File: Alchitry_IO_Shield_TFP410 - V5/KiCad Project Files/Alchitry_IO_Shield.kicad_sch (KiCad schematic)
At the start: 1 part, among them U1 boardmezzanine_new

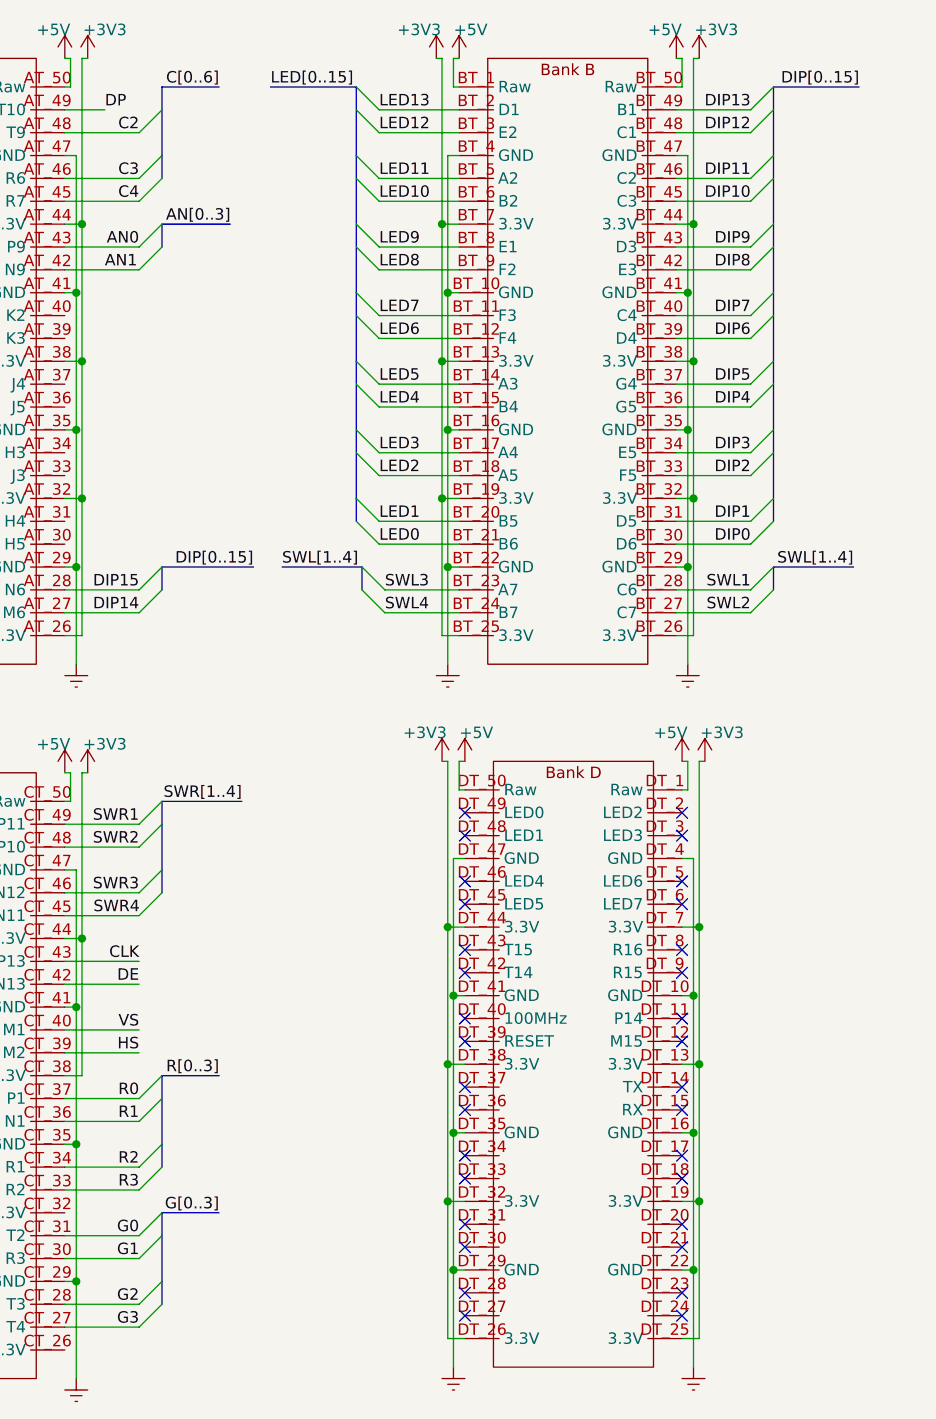
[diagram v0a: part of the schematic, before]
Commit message: grouped footprints by function
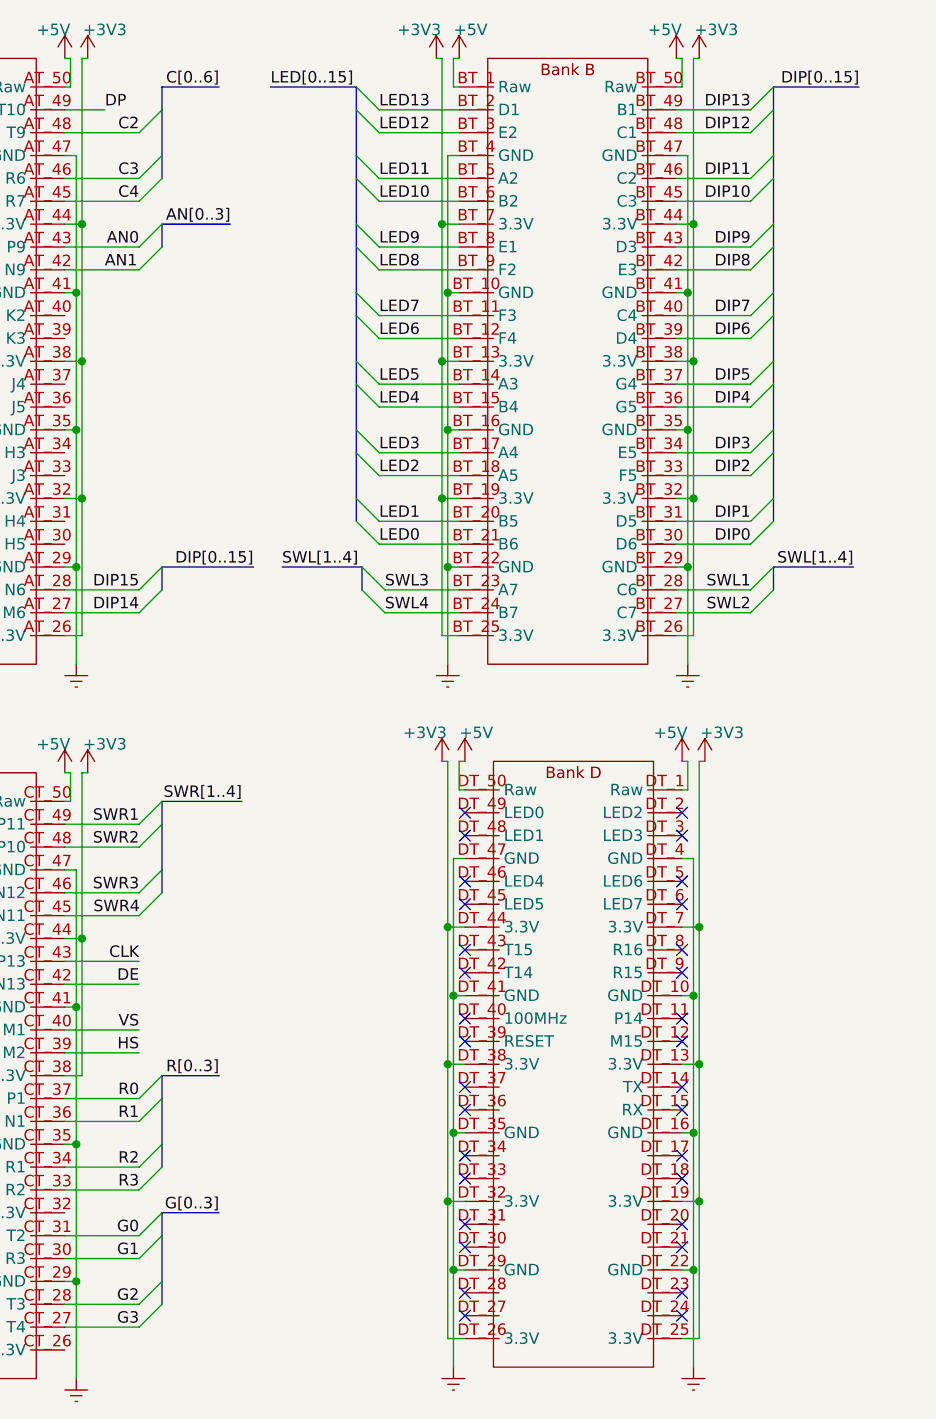
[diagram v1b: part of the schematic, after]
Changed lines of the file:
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@@
-(kicad_sch (version 20200714) (host eeschema "(5.99.0-2326-ge7e1d5140)")
+(kicad_sch (version 20200714) (host eeschema "(5.99.0-2416-g010316457)")
   (page 1 3)
   (paper "A4")
@@
   (junction (at 135.255 129.54) (diameter 0) (color 0 0 0 0))
   (junction (at 135.255 144.78) (diameter 0) (color 0 0 0 0))
+  (no_connect (at 133.35 111.76))
+  (no_connect (at 133.35 104.14))
+  (no_connect (at 109.22 119.38))
+  (no_connect (at 40.64 143.51))
+  (no_connect (at 133.35 116.84))
+  (no_connect (at 109.22 104.14))
+  (no_connect (at 133.35 157.48))
+  (no_connect (at 40.64 133.35))
+  (no_connect (at 109.22 124.46))
+  (no_connect (at 109.22 132.08))
+  (no_connect (at 109.22 134.62))
+  (no_connect (at 109.22 109.22))
+  (no_connect (at 40.64 140.97))
+  (no_connect (at 109.22 101.6))
+  (no_connect (at 133.35 147.32))
+  (no_connect (at 40.64 102.87))
+  (no_connect (at 109.22 157.48))
+  (no_connect (at 109.22 154.94))
   (no_connect (at 133.35 134.62))
+  (no_connect (at 133.35 132.08))
+  (no_connect (at 133.35 101.6))
+  (no_connect (at 109.22 149.86))
+  (no_connect (at 109.22 127))
+  (no_connect (at 133.35 127))
   (no_connect (at 40.64 120.65))
-  (no_connect (at 109.22 127))
-  (no_connect (at 133.35 111.76))
-  (no_connect (at 133.35 132.08))
+  (no_connect (at 109.22 116.84))
+  (no_connect (at 133.35 124.46))
+  (no_connect (at 40.64 125.73))
+  (no_connect (at 40.64 113.03))
   (no_connect (at 40.64 128.27))
+  (no_connect (at 133.35 119.38))
+  (no_connect (at 40.64 135.89))
+  (no_connect (at 133.35 149.86))
+  (no_connect (at 40.64 118.11))
+  (no_connect (at 133.35 154.94))
+  (no_connect (at 40.64 110.49))
+  (no_connect (at 133.35 139.7))
+  (no_connect (at 40.64 105.41))
+  (no_connect (at 133.35 142.24))
+  (no_connect (at 109.22 139.7))
   (no_connect (at 109.22 147.32))
+  (no_connect (at 109.22 142.24))
   (no_connect (at 109.22 111.76))
-  (no_connect (at 133.35 157.48))
-  (no_connect (at 109.22 116.84))
-  (no_connect (at 133.35 142.24))
   (no_connect (at 133.35 109.22))
-  (no_connect (at 109.22 139.7))
-  (no_connect (at 40.64 110.49))
-  (no_connect (at 133.35 101.6))
-  (no_connect (at 109.22 142.24))
-  (no_connect (at 133.35 119.38))
-  (no_connect (at 109.22 104.14))
-  (no_connect (at 109.22 154.94))
-  (no_connect (at 40.64 118.11))
-  (no_connect (at 109.22 119.38))
-  (no_connect (at 109.22 134.62))
-  (no_connect (at 133.35 116.84))
-  (no_connect (at 40.64 102.87))
-  (no_connect (at 40.64 133.35))
-  (no_connect (at 40.64 125.73))
-  (no_connect (at 133.35 124.46))
-  (no_connect (at 40.64 140.97))
-  (no_connect (at 109.22 132.08))
-  (no_connect (at 133.35 149.86))
-  (no_connect (at 133.35 104.14))
-  (no_connect (at 40.64 113.03))
-  (no_connect (at 133.35 154.94))
-  (no_connect (at 133.35 127))
-  (no_connect (at 109.22 157.48))
-  (no_connect (at 109.22 101.6))
-  (no_connect (at 40.64 143.51))
-  (no_connect (at 109.22 149.86))
-  (no_connect (at 109.22 124.46))
-  (no_connect (at 40.64 105.41))
-  (no_connect (at 133.35 139.7))
-  (no_connect (at 40.64 135.89))
-  (no_connect (at 133.35 147.32))
-  (no_connect (at 109.22 109.22))
   (bus_entry (at 29.21 20.955) (size 2.54 2.54)
     (stroke (width 0.1524) (type solid) (color 0 0 0 0))
@@
     (stroke (width 0) (type solid) (color 0 0 0 0))
   )
-  (bus (pts (xy 75.565 20.955) (xy 75.565 28.575))
+  (bus (pts (xy 75.565 20.955) (xy 75.565 23.495))
     (stroke (width 0) (type solid) (color 0 0 0 0))
   )
@@
     (stroke (width 0) (type solid) (color 0 0 0 0))
   )
-  (bus (pts (xy 75.565 28.575) (xy 75.565 31.115))
+  (bus (pts (xy 75.565 23.495) (xy 75.565 31.115))
     (stroke (width 0) (type solid) (color 0 0 0 0))
   )
@@
     (stroke (width 0) (type solid) (color 0 0 0 0))
   )
-  (bus (pts (xy 75.565 100.33) (xy 75.565 102.87))
+  (bus (pts (xy 75.565 100.33) (xy 75.565 107.95))
     (stroke (width 0) (type solid) (color 0 0 0 0))
   )
@@
     (stroke (width 0) (type solid) (color 0 0 0 0))
   )
-  (bus (pts (xy 75.565 102.87) (xy 75.565 110.49))
-    (stroke (width 0) (type solid) (color 0 0 0 0))
-  )
-  (bus (pts (xy 75.565 130.81) (xy 75.565 138.43))
+  (bus (pts (xy 75.565 107.95) (xy 75.565 110.49))
+    (stroke (width 0) (type solid) (color 0 0 0 0))
+  )
+  (bus (pts (xy 75.565 130.81) (xy 75.565 133.35))
     (stroke (width 0) (type solid) (color 0 0 0 0))
   )
@@
     (stroke (width 0) (type solid) (color 0 0 0 0))
   )
-  (bus (pts (xy 75.565 138.43) (xy 75.565 140.97))
-    (stroke (width 0) (type solid) (color 0 0 0 0))
-  )
-  (bus (pts (xy 75.565 146.05) (xy 75.565 153.67))
+  (bus (pts (xy 75.565 133.35) (xy 75.565 140.97))
+    (stroke (width 0) (type solid) (color 0 0 0 0))
+  )
+  (bus (pts (xy 75.565 146.05) (xy 75.565 148.59))
     (stroke (width 0) (type solid) (color 0 0 0 0))
   )
@@
     (stroke (width 0) (type solid) (color 0 0 0 0))
   )
-  (bus (pts (xy 75.565 153.67) (xy 75.565 156.21))
+  (bus (pts (xy 75.565 148.59) (xy 75.565 156.21))
     (stroke (width 0) (type solid) (color 0 0 0 0))
   )
@@
     (stroke (width 0) (type solid) (color 0 0 0 0))
   )
-  (bus (pts (xy 97.155 43.815) (xy 97.155 51.435))
-    (stroke (width 0) (type solid) (color 0 0 0 0))
-  )
-  (bus (pts (xy 97.155 51.435) (xy 97.155 59.055))
-    (stroke (width 0) (type solid) (color 0 0 0 0))
-  )
-  (bus (pts (xy 97.155 59.055) (xy 97.155 66.675))
-    (stroke (width 0) (type solid) (color 0 0 0 0))
-  )
-  (bus (pts (xy 97.155 66.675) (xy 97.155 69.215))
+  (bus (pts (xy 97.155 43.815) (xy 97.155 46.355))
+    (stroke (width 0) (type solid) (color 0 0 0 0))
+  )
+  (bus (pts (xy 97.155 46.355) (xy 97.155 53.975))
+    (stroke (width 0) (type solid) (color 0 0 0 0))
+  )
+  (bus (pts (xy 97.155 53.975) (xy 97.155 61.595))
+    (stroke (width 0) (type solid) (color 0 0 0 0))
+  )
+  (bus (pts (xy 97.155 61.595) (xy 97.155 69.215))
     (stroke (width 0) (type solid) (color 0 0 0 0))
   )
@@
     (stroke (width 0) (type solid) (color 0 0 0 0))
   )
-  (bus (pts (xy 143.51 43.815) (xy 143.51 46.355))
-    (stroke (width 0) (type solid) (color 0 0 0 0))
-  )
-  (bus (pts (xy 143.51 46.355) (xy 143.51 53.975))
-    (stroke (width 0) (type solid) (color 0 0 0 0))
-  )
-  (bus (pts (xy 143.51 53.975) (xy 143.51 61.595))
-    (stroke (width 0) (type solid) (color 0 0 0 0))
-  )
+  (bus (pts (xy 143.51 43.815) (xy 143.51 51.435))
+    (stroke (width 0) (type solid) (color 0 0 0 0))
+  )
+  (bus (pts (xy 143.51 51.435) (xy 143.51 59.055))
+    (stroke (width 0) (type solid) (color 0 0 0 0))
+  )
+  (bus (pts (xy 143.51 59.055) (xy 143.51 61.595))
+    (stroke (width 0) (type solid) (color 0 0 0 0))
+  )

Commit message: started new shield
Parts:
- removed U1: boardmezzanine_new, Custom_Parts:Alchitry_Top_Bottom, symbol Custom_Symbols:Adaptor_both-alchitry_symbols
- added U1: Alchitry_Single, Alchitry_Footprints:Alchitry_Bottom, symbol Alchitry_Symbols:Alchitry_Single
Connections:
- net +3V3: now also U1.A_13 (3.3V), U1.A_19 (3.3V), U1.A_25 (3.3V), U1.A_26 (3.3V), U1.A_32 (3.3V), U1.A_38 (3.3V), U1.A_42 (N9), U1.A_44 (3.3V), U1.A_7 (3.3V), U1.B_13 (3.3V), U1.B_19 (3.3V), U1.B_25 (3.3V), U1.B_26 (3.3V), U1.B_32 (3.3V), U1.B_38 (3.3V), U1.B_44 (3.3V), U1.B_7 (3.3V), U1.C_13 (3.3V), U1.C_19 (3.3V), U1.C_25 (3.3V), U1.C_26 (3.3V), U1.C_32 (3.3V), U1.C_38 (3.3V), U1.C_44 (3.3V), U1.C_7 (3.3V), U1.D_13 (3.3V), U1.D_19 (3.3V), U1.D_25 (3.3V), U1.D_26 (3.3V), U1.D_32 (3.3V), U1.D_38 (3.3V), U1.D_44 (3.3V), U1.D_7 (3.3V)
- net +5V: now also U1.A_1 (Raw), U1.A_50 (Raw), U1.B_1 (Raw), U1.B_50 (Raw), U1.C_1 (Raw), U1.C_50 (Raw), U1.D_1 (Raw), U1.D_50 (Raw)
- net AN0: now also U1.A_43 (P9)
- net AN2: now also U1.A_8 (R8)
- net AN3: now also U1.A_9 (P8)
- net B0: now also U1.C_20 (N4)
- net B1: now also U1.C_21 (M5)
- net B2: now also U1.C_23 (L5)
- net B3: now also U1.C_24 (P5)
- net C0: now also U1.A_5 (T5)
- net C1: now also U1.A_6 (R5)
- net C2: now also U1.A_48 (T9)
- net C3: now also U1.A_46 (R6)
- net C4: now also U1.A_45 (R7)
- net C5: now also U1.A_3 (T7)
- net C6: now also U1.A_2 (T8)
- net CLK: now also U1.C_43 (P13)
- net DE: now also U1.C_42 (N13)
- net DIP0: now also U1.B_30 (D6)
- net DIP1: now also U1.B_31 (D5)
- net DIP10: now also U1.B_45 (C3)
- net DIP11: now also U1.B_46 (C2)
- net DIP12: now also U1.B_48 (C1)
- net DIP13: now also U1.B_49 (B1)
- net DIP14: now also U1.A_27 (M6)
- net DIP15: now also U1.A_28 (N6)
- net DIP2: now also U1.B_33 (F5)
- net DIP3: now also U1.B_34 (E5)
- net DIP4: now also U1.B_36 (G5)
- net DIP5: now also U1.B_37 (G4)
- net DIP6: now also U1.B_39 (D4)
- net DIP7: now also U1.B_40 (C4)
- net DIP8: now also U1.B_42 (E3)
- net DIP9: now also U1.B_43 (D3)
- net DP: now also U1.A_49 (T10)
- net G0: now also U1.C_31 (T2)
- net G1: now also U1.C_30 (R3)
- net G2: now also U1.C_28 (T3)
- net G3: now also U1.C_27 (T4)
- net GNDREF: now also U1.A_10 (GND), U1.A_16 (GND), U1.A_22 (GND), U1.A_29 (GND), U1.A_35 (GND), U1.A_4 (GND), U1.A_41 (GND), U1.A_47 (GND), U1.B_10 (GND), U1.B_16 (GND), U1.B_22 (GND), U1.B_29 (GND), U1.B_35 (GND), U1.B_4 (GND), U1.B_41 (GND), U1.B_47 (GND), U1.C_10 (GND), U1.C_16 (GND), U1.C_22 (GND), U1.C_29 (GND), U1.C_35 (GND), U1.C_4 (GND), U1.C_41 (GND), U1.C_47 (GND), U1.D_10 (GND), U1.D_16 (GND), U1.D_22 (GND), U1.D_29 (GND), U1.D_35 (GND), U1.D_4 (GND), U1.D_41 (GND), U1.D_47 (GND)
- net HS: now also U1.C_39 (M2)
- net LED0: now also U1.B_21 (B6)
- net LED1: now also U1.B_20 (B5)
- net LED10: now also U1.B_6 (B2)
- net LED11: now also U1.B_5 (A2)
- net LED12: now also U1.B_3 (E2)
- net LED13: now also U1.B_2 (D1)
- net LED14: now also U1.A_24 (E6)
- net LED15: now also U1.A_23 (K5)
- net LED2: now also U1.B_18 (A5)
- net LED3: now also U1.B_17 (A4)
- net LED4: now also U1.B_15 (B4)
- net LED5: now also U1.B_14 (A3)
- net LED6: now also U1.B_12 (F4)
- net LED7: now also U1.B_11 (F3)
- net LED8: now also U1.B_9 (F2)
- net LED9: now also U1.B_8 (E1)
- net R0: now also U1.C_37 (P1)
- net R1: now also U1.C_36 (N1)
- net R2: now also U1.C_34 (R1)
- net R3: now also U1.C_33 (R2)
- net SWL1: now also U1.B_28 (C6)
- net SWL2: now also U1.B_27 (C7)
- net SWL3: now also U1.B_23 (A7)
- net SWL4: now also U1.B_24 (B7)
- net SWR1: now also U1.C_46 (N12)
- net SWR2: now also U1.C_49 (P11)
- net SWR3: now also U1.C_48 (P10)
- net SWR4: now also U1.C_45 (N11)
- net VS: now also U1.C_40 (M1)

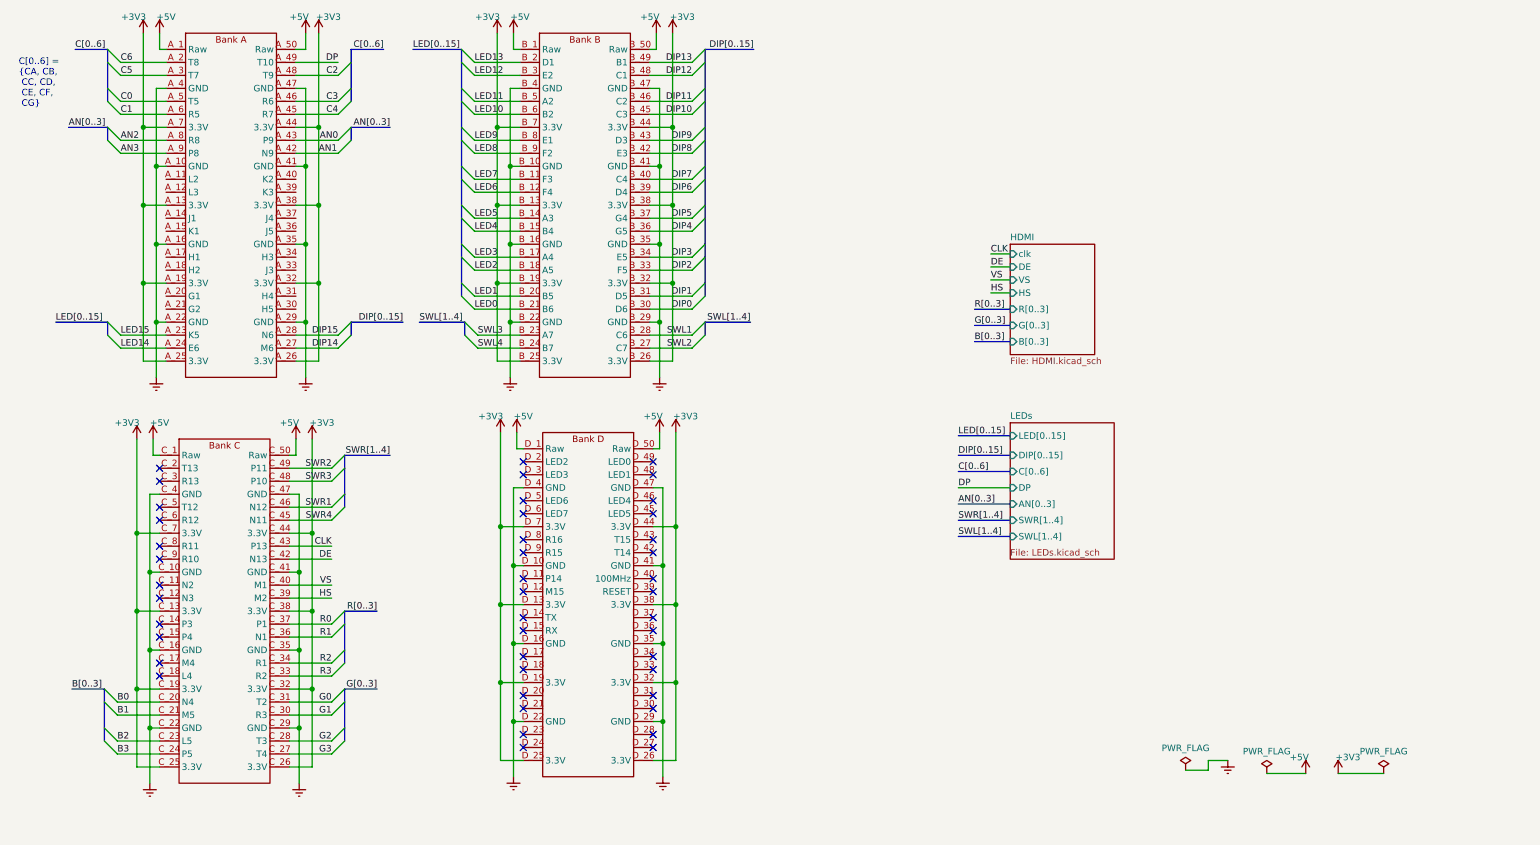
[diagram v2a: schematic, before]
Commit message: replaced 7segs with custom footprints
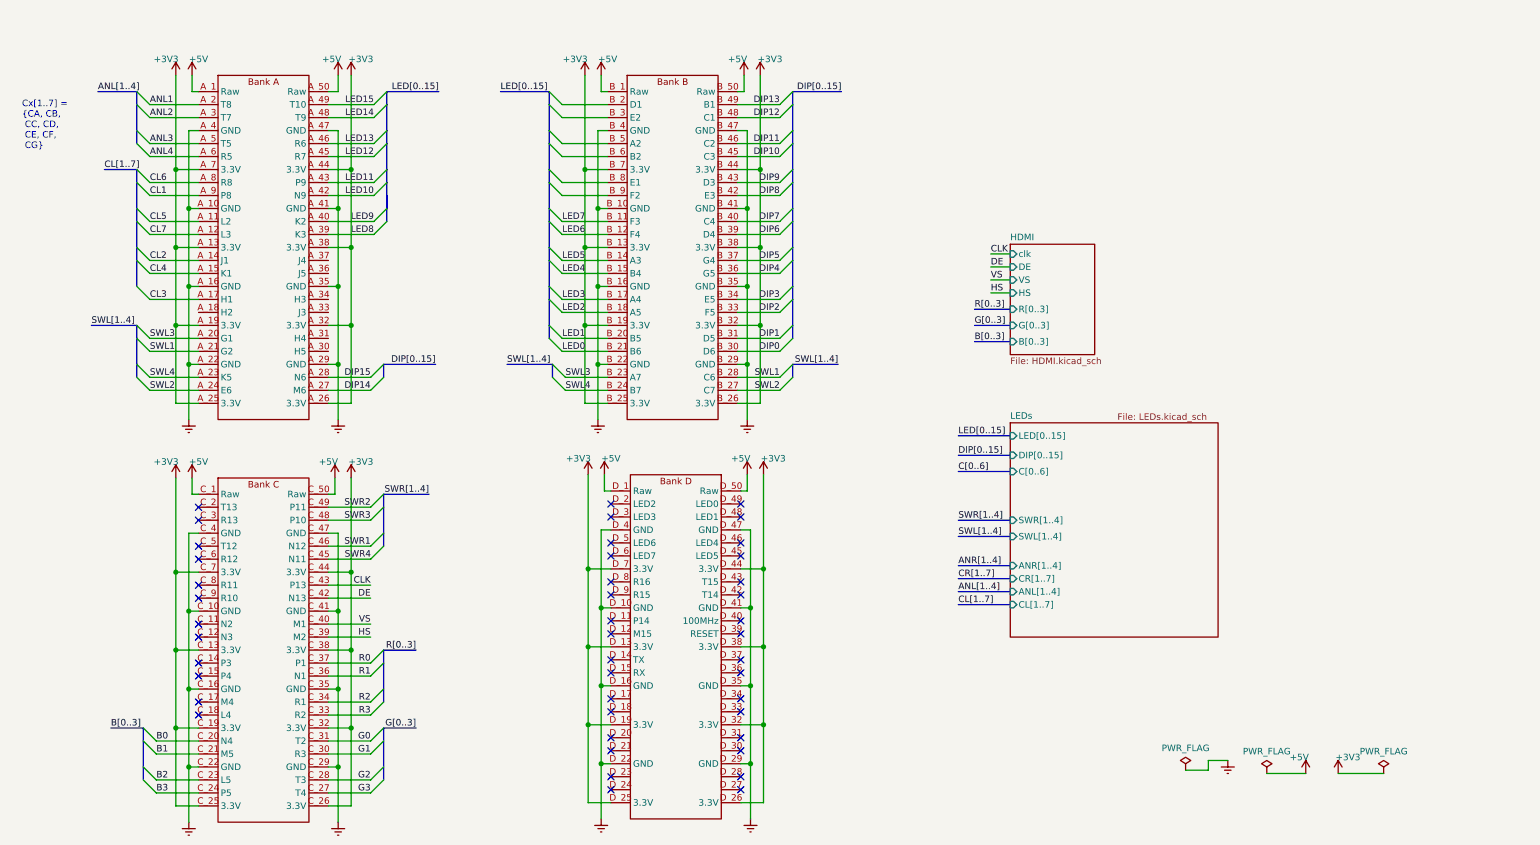
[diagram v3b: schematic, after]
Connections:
- net AN0 is gone; now on net LED11: U1.A_43 (P9)
- net C2 is gone; now on net LED14: U1.A_48 (T9)
- net C3 is gone; now on net LED13: U1.A_46 (R6)
- net C4 is gone; now on net LED12: U1.A_45 (R7)
- net DP is gone; now on net LED15: U1.A_49 (T10)
- net +3V3: no longer U1.A_42 (N9)
- net LED10: now also U1.A_42 (N9); no longer U1.B_6 (B2)
- net LED11: no longer U1.B_5 (A2)
- net LED12: no longer U1.B_3 (E2)
- net LED13: no longer U1.B_2 (D1)
- net LED14: no longer U1.A_24 (E6)
- net LED15: no longer U1.A_23 (K5)
- net LED8: now also U1.A_39 (K3); no longer U1.B_9 (F2)
- net LED9: now also U1.A_40 (K2); no longer U1.B_8 (E1)
- net SWL1: now also U1.A_21 (G2)
- net SWL2: now also U1.A_24 (E6)
- net SWL3: now also U1.A_20 (G1)
- net SWL4: now also U1.A_23 (K5)
- net CL5: now reaches U1.A_11 (L2)
- net CL7: now reaches U1.A_12 (L3)
- net CL2: now reaches U1.A_14 (J1)
- net CL4: now reaches U1.A_15 (K1)
- net CL3: now reaches U1.A_17 (H1)
- net AN2 renamed CL6
- net AN3 renamed CL1
- net C0 renamed ANL3
- net C1 renamed ANL4
- net C5 renamed ANL2
- net C6 renamed ANL1
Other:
- sheet LEDs ports: added ANL[1..4], ANR[1..4], CL[1..7], CR[1..7]; removed AN[0..3], DP
- note added: "Cx[1..7] = {CA, CB, CC, CD, CE, CF, CG}"
- note removed: "C[0..6] = {CA, CB, CC, CD, CE, CF, CG}"
